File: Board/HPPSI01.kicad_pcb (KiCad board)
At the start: 2 copper layers, 75 x 80.6 mm, 43 parts, among them J1 Conn_02x05_Odd_Even, J10 Conn_02x05_Odd_Even, J2 Conn_02x05_Odd_Even, J3 Conn_02x05_Odd_Even, J4 Conn_02x05_Odd_Even, J5 Conn_02x05_Odd_Even, J6 Conn_02x05_Odd_Even, J7 Conn_02x05_Odd_Even, J8 Conn_02x05_Odd_Even, J9 Conn_02x05_Odd_Even, U1 MAX4617EUE+, U10 MAX4617EUE+, U11 Digilent-CoraZ7_units, U2 MAX4617EUE+, U3 MAX4617EUE+, U4 MAX4617EUE+, U5 MAX4617EUE+, U6 MAX4617EUE+, U7 MAX4617EUE+, U8 MAX4617EUE+, U9 MAX4617EUE+

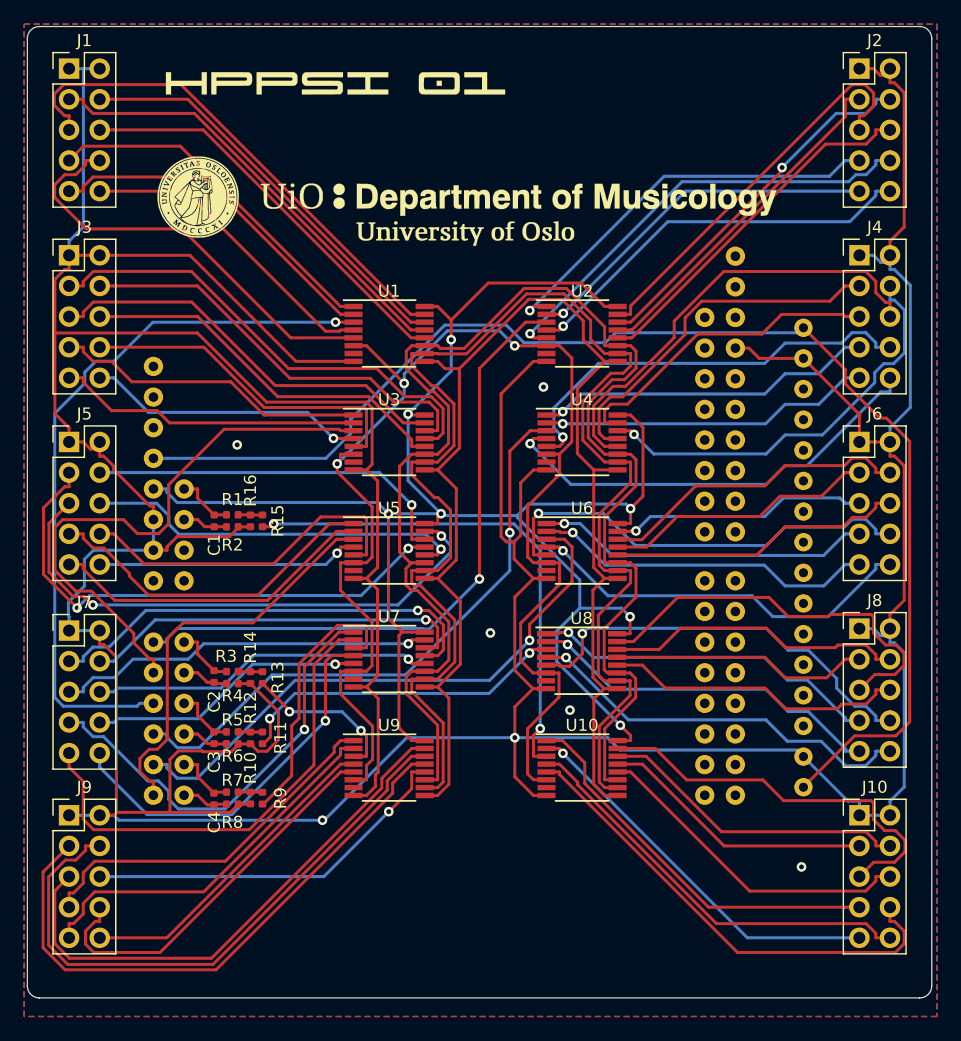
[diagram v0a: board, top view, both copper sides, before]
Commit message: added 3D object in wrl format
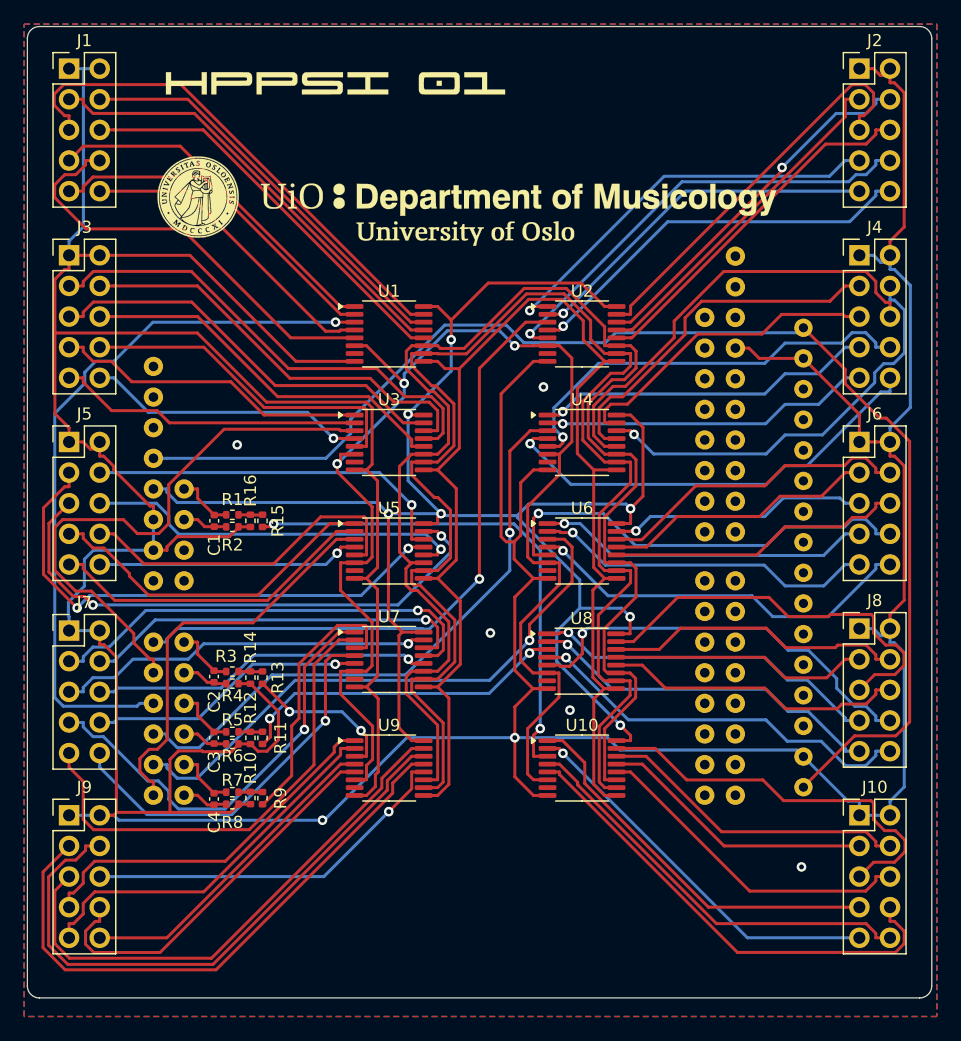
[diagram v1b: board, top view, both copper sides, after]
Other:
- net class Default removed
